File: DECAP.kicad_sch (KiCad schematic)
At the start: 0 parts

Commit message: Saving before changing RAM from DDR3 to Parallel SDR SRAM
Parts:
- added C17, C19, C20, C21, C22, C27, C28, C31, C32, C49, C50, C51: 100nF, symbol Device:C
- added C18, C23, C24, C25, C26, C29, C30, C47, C48, C52, C53, C54: 10nF, symbol Device:C
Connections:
- new net GND: C17.2, C18.2, C19.2, C20.2, C21.2, C22.2, C23.2, C24.2, C25.2, C26.2, C27.2, C28.2, C29.2, C30.2, C31.2, C32.2, C47.2, C48.2, C49.2, C50.2, C51.2, C52.2, C53.2, C54.2
- new net P1V1: C17.1, C18.1, C19.1, C20.1, C21.1, C22.1, C23.1, C24.1, C25.1, C26.1
- new net P1V35: C31.1, C32.1, C47.1, C48.1
- new net P2V5: C27.1, C28.1, C29.1, C30.1
- new net P3V3: C49.1, C50.1, C51.1, C52.1, C53.1, C54.1

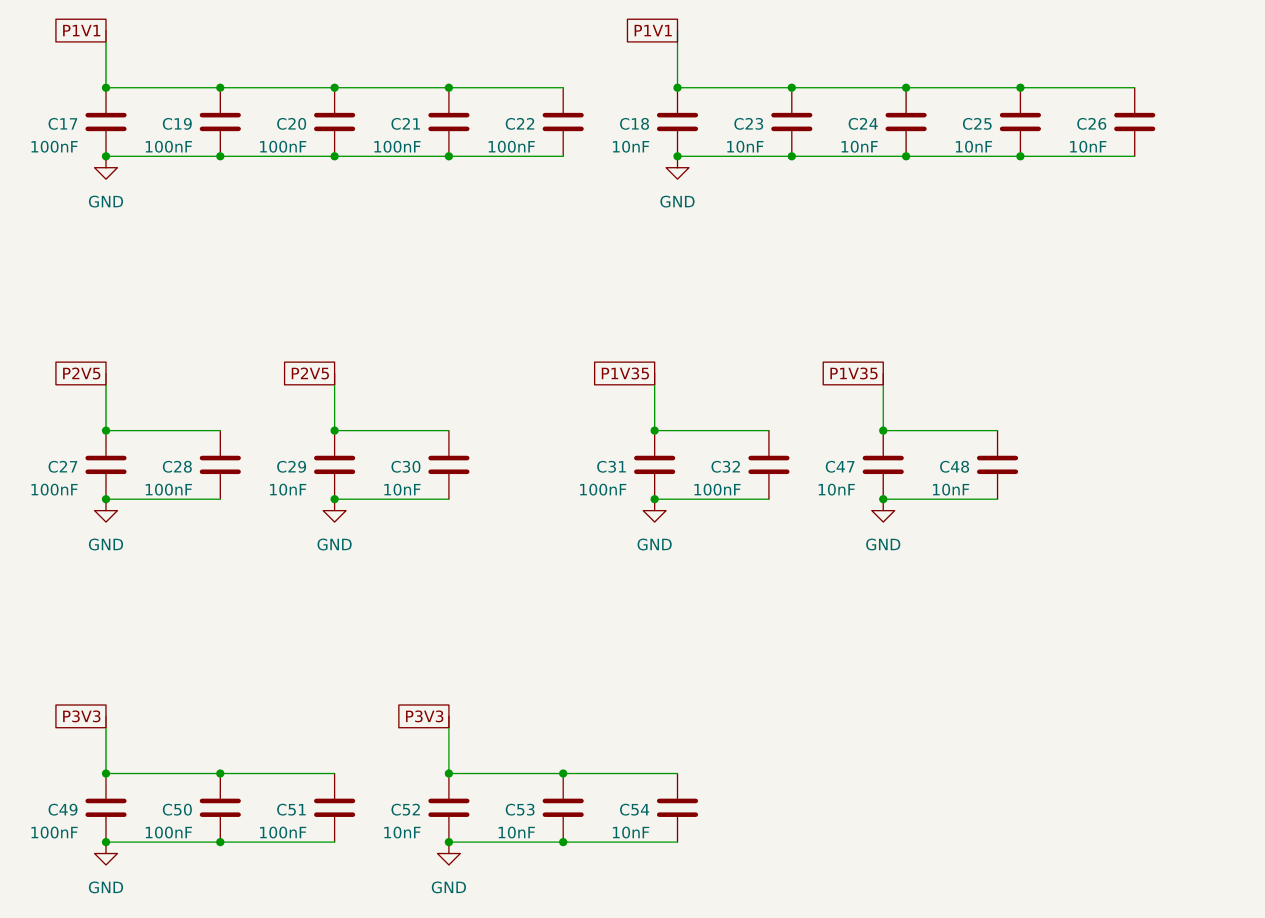
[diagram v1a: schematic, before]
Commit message: Added more I/O. Changed power regulators
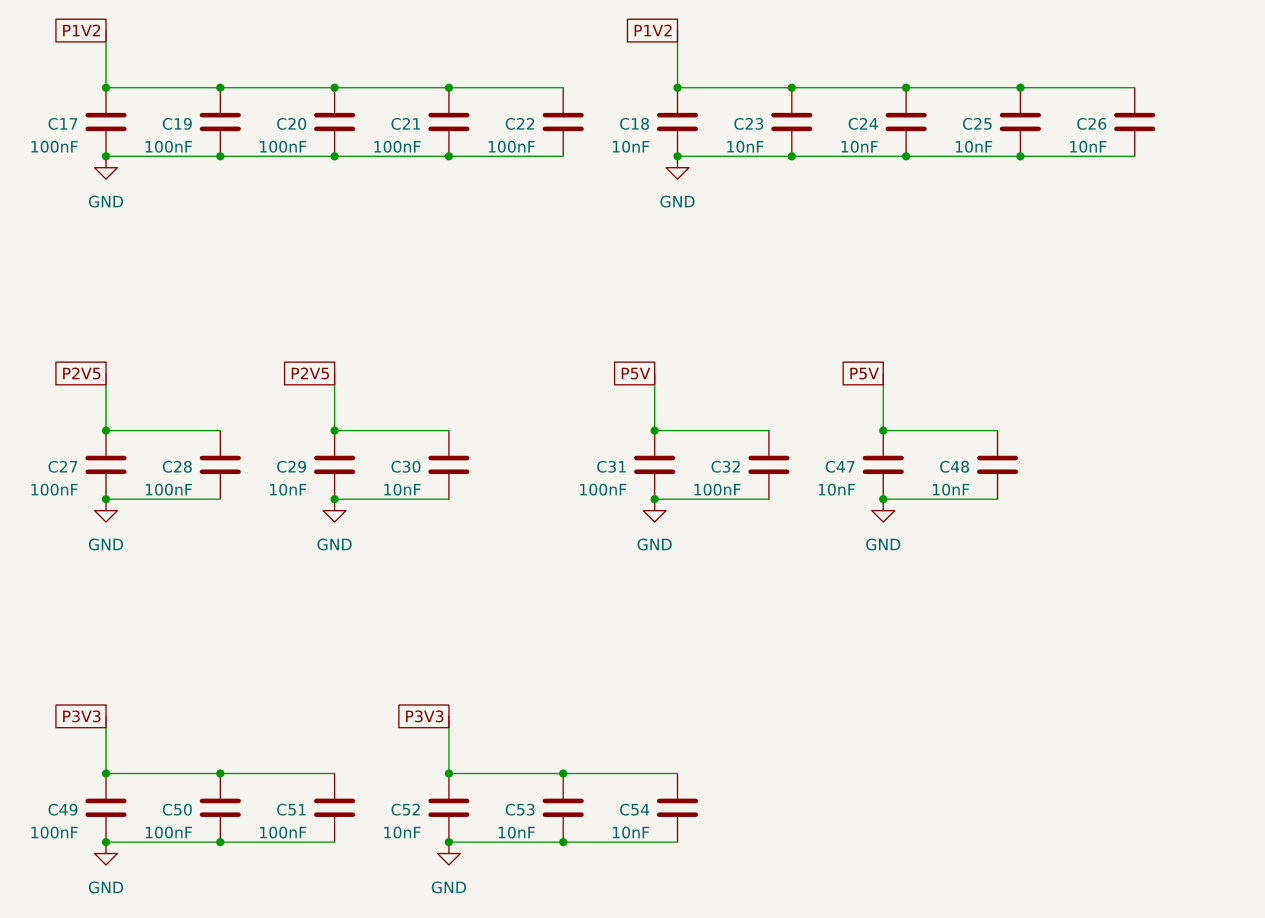
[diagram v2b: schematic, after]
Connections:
- net P1V1 renamed P1V2
- net P1V35 renamed P5V
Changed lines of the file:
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@@
 		)
 	)
-	(global_label "P1V1"
+	(global_label "P1V2"
 		(shape passive)
 		(at 127 44.45 180)
@@
 		)
 	)
-	(global_label "P1V35"
+	(global_label "P5V"
 		(shape passive)
 		(at 124.46 82.55 180)
@@
 		)
 		(property "Intersheetrefs" "${INTERSHEET_REFS}"
-			(at 116.599 82.55 0)
+			(at 119.018 82.55 0)
 			(effects
 				(font
@@
 		)
 	)
-	(global_label "P1V35"
+	(global_label "P5V"
 		(shape passive)
 		(at 149.86 82.55 180)
@@
 		)
 		(property "Intersheetrefs" "${INTERSHEET_REFS}"
-			(at 141.999 82.55 0)
+			(at 144.418 82.55 0)
 			(effects
 				(font
@@
 		)
 	)
-	(global_label "P1V1"
+	(global_label "P1V2"
 		(shape passive)
 		(at 63.5 44.45 180)

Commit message: Power routed. Saving before reworking ICE40 pins to optimize layout
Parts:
- added C11: 100nF, Capacitor_SMD:C_0603_1608Metric, symbol Device:C
- added C12: 10nF, Capacitor_SMD:C_0603_1608Metric, symbol Device:C
- added C62, C63: 2.2uF, Capacitor_SMD:C_0603_1608Metric, symbol Device:C
- C17, C18, C19, C20, C21, C22, C23, C24, C25, C26, C27, C28, C29, C30, C31, C32, C47, C48, C49, C50, C51, C52, C53, C54: footprint (none) -> Capacitor_SMD:C_0603_1608Metric
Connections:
- net GND: now also C11.2, C12.2, C62.2, C63.2
- net P3V3: now also C11.1, C12.1
- net P5V renamed USB_VBUS2
- net USB_VBUS2: now also C62.1, C63.1
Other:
- moved on the sheet: C52, C53, C54
